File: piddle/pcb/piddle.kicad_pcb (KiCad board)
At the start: 2 copper layers, 139.2 x 138.5 mm, 87 parts, among them J1 Conn_01x03_Socket, J10 Conn_01x03_Socket, J11 Conn_01x03_Socket, J12 Conn_01x03_Socket, J13 Conn_01x03_Socket, J14 Conn_01x03_Socket, J15 Conn_01x03_Socket, J16 infrared receiver, J17 5v power, J18 3v3 power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

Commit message: Connect all components
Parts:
- added J25: JST power 3, Connector_JST:JST_PH_S2B-PH-K_1x02_P2.00mm_Horizontal, F.Cu at (41.7, 80.7)
- J17, J19: value 5v power -> 5v
- J18: value 3v3 power -> 3v3
- J22: renamed from LED v jumper
- moved J22 80.3 mm to (98.6, 136.6), turned to 90 degrees
- moved J21 50.8 mm to (146.6, 60.6), turned to 132 degrees
- moved R13 5.00 mm to (70.3, 126.8)
- moved R2 5.00 mm to (129.7, 126.8)
- moved R15 5.00 mm to (100.0, 140.0)
- moved R6 5.00 mm to (123.5, 67.6)
- moved R9 5.00 mm to (76.5, 67.6)
- moved R11 5.00 mm to (60.2, 95.8)
- moved R4 5.00 mm to (139.8, 95.8)
- moved R5 5.00 mm to (134.6, 80.0)
- moved R10 5.00 mm to (65.4, 80.0)
- moved R7 5.00 mm to (108.3, 60.9)
- moved R8 5.00 mm to (91.7, 60.9)
- moved R1 5.00 mm to (116.3, 136.5)
- moved R14 5.00 mm to (83.7, 136.5)
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- renumbered 34 to J23
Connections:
- J23 pad 1: /GPIO34 -> /GPIO35
- J23 pad 2: /GPIO39 -> /GPIO34
- J4 pad 2: Net-(D4-DIN) -> Net-(D4-DOUT)
- J6 pad 2: Net-(D6-DIN) -> Net-(D6-DOUT)
- R4 pad 2: Net-(D4-DOUT) -> Net-(D4-DIN)
- R6 pad 2: Net-(D6-DOUT) -> Net-(D6-DIN)
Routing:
- net /4.3V: track 0.00 -> 451.9 mm
- net +5V: track 0.00 -> 280.0 mm
- net +3.3V: track 0.00 -> 74.9 mm
- net /GPIO19: track 0.00 -> 49.5 mm
- net /GPIO21: track 0.00 -> 47.5 mm
- net /GPIO18: track 0.00 -> 46.3 mm
- net /GPIO35: track 0.00 -> 44.4 mm
- net /GPIO36: track 0.00 -> 42.0 mm
- net /GPIO5: track 0.00 -> 41.3 mm
- net /GPIO34: track 0.00 -> 40.8 mm
- net /GPIO33: track 0.00 -> 39.2 mm
- net /GPIO32: track 0.00 -> 39.0 mm
- net /GPIO25: track 0.00 -> 35.3 mm
- net /GPIO17: track 0.00 -> 34.1 mm
- net /GPIO39: track 0.00 -> 30.3 mm
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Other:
- board text added: "34"
- board text added: "35"
- board text added: "Brandon Skari"
- board text added: "LED v"
- board text added: "Phonic Bloom 2.0"
- board text added: "Phonic Bloom 2.0 Brandon Skari github.com/apogaea/piddle"
- board text added: "github.com/apogaea/piddle"

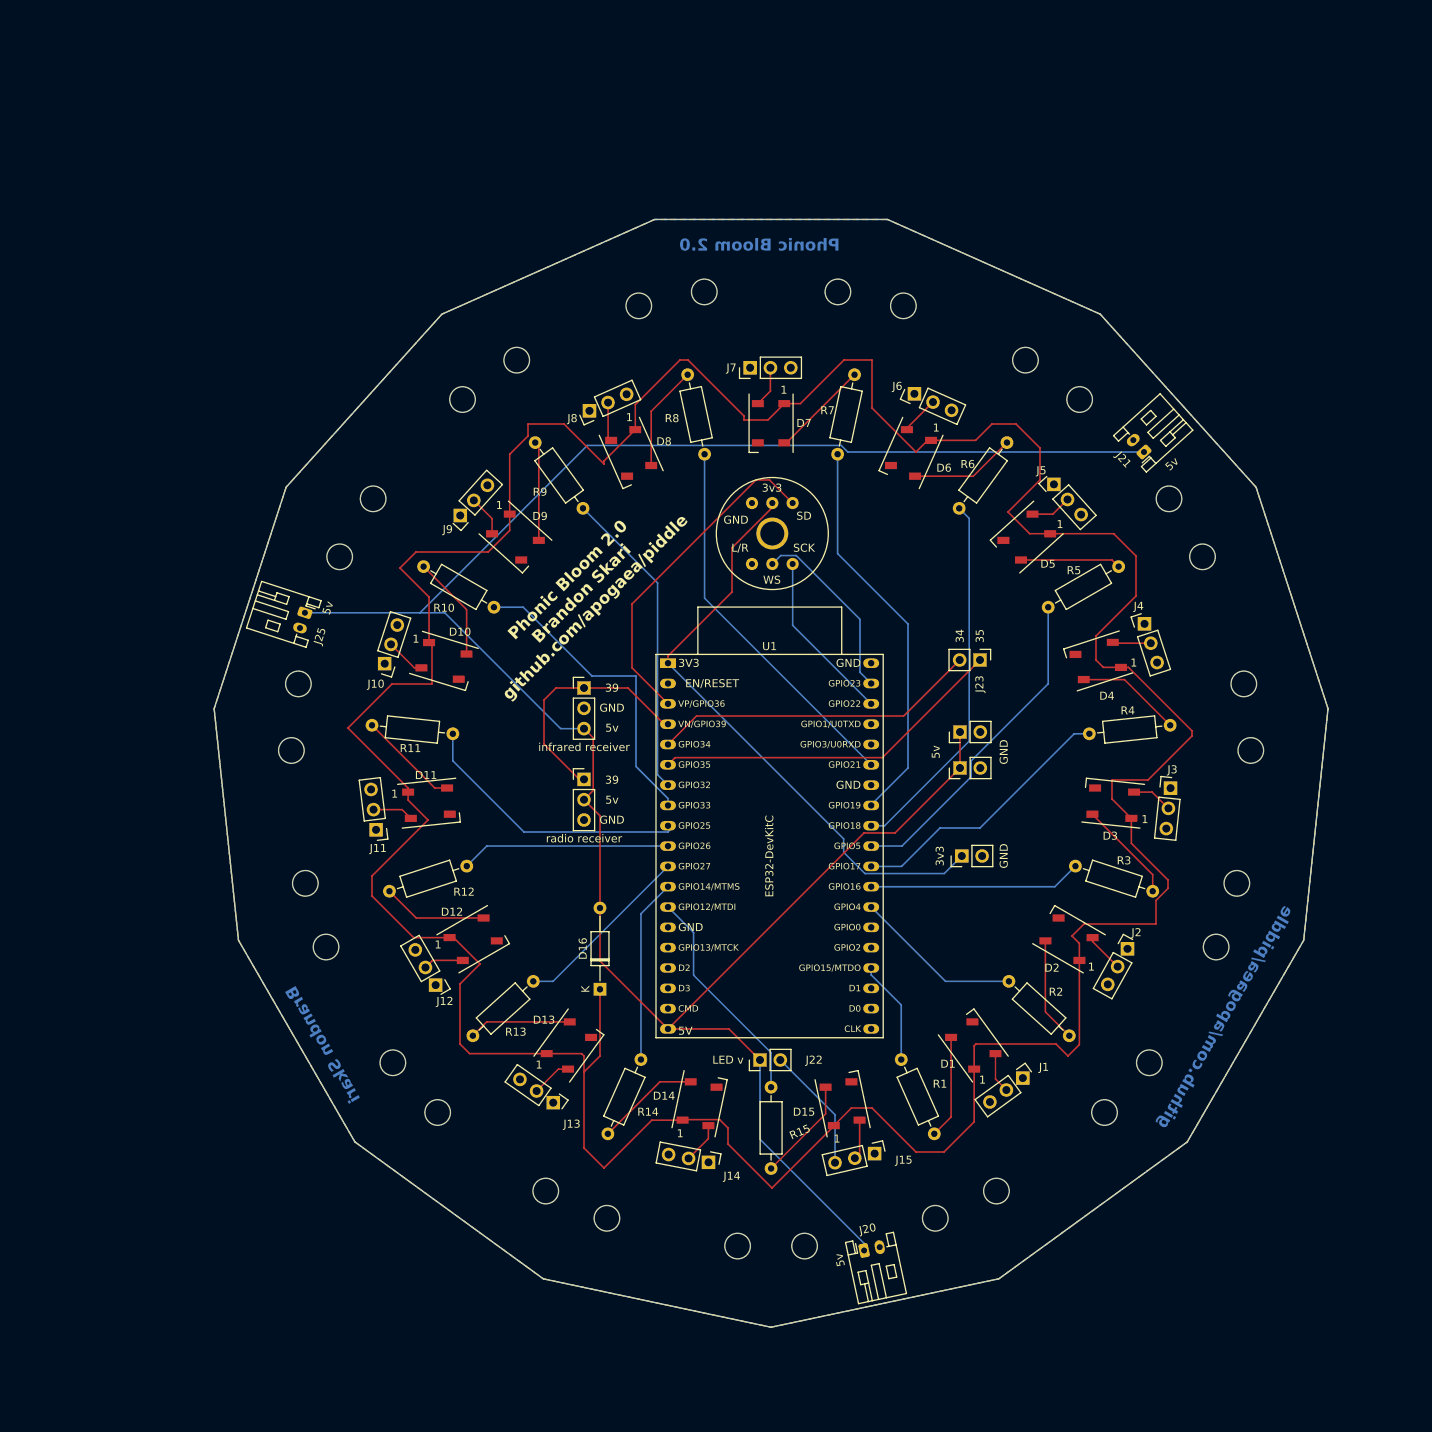
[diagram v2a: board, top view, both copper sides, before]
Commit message: Rotate LED solder pads and update to workwith KiCad 9
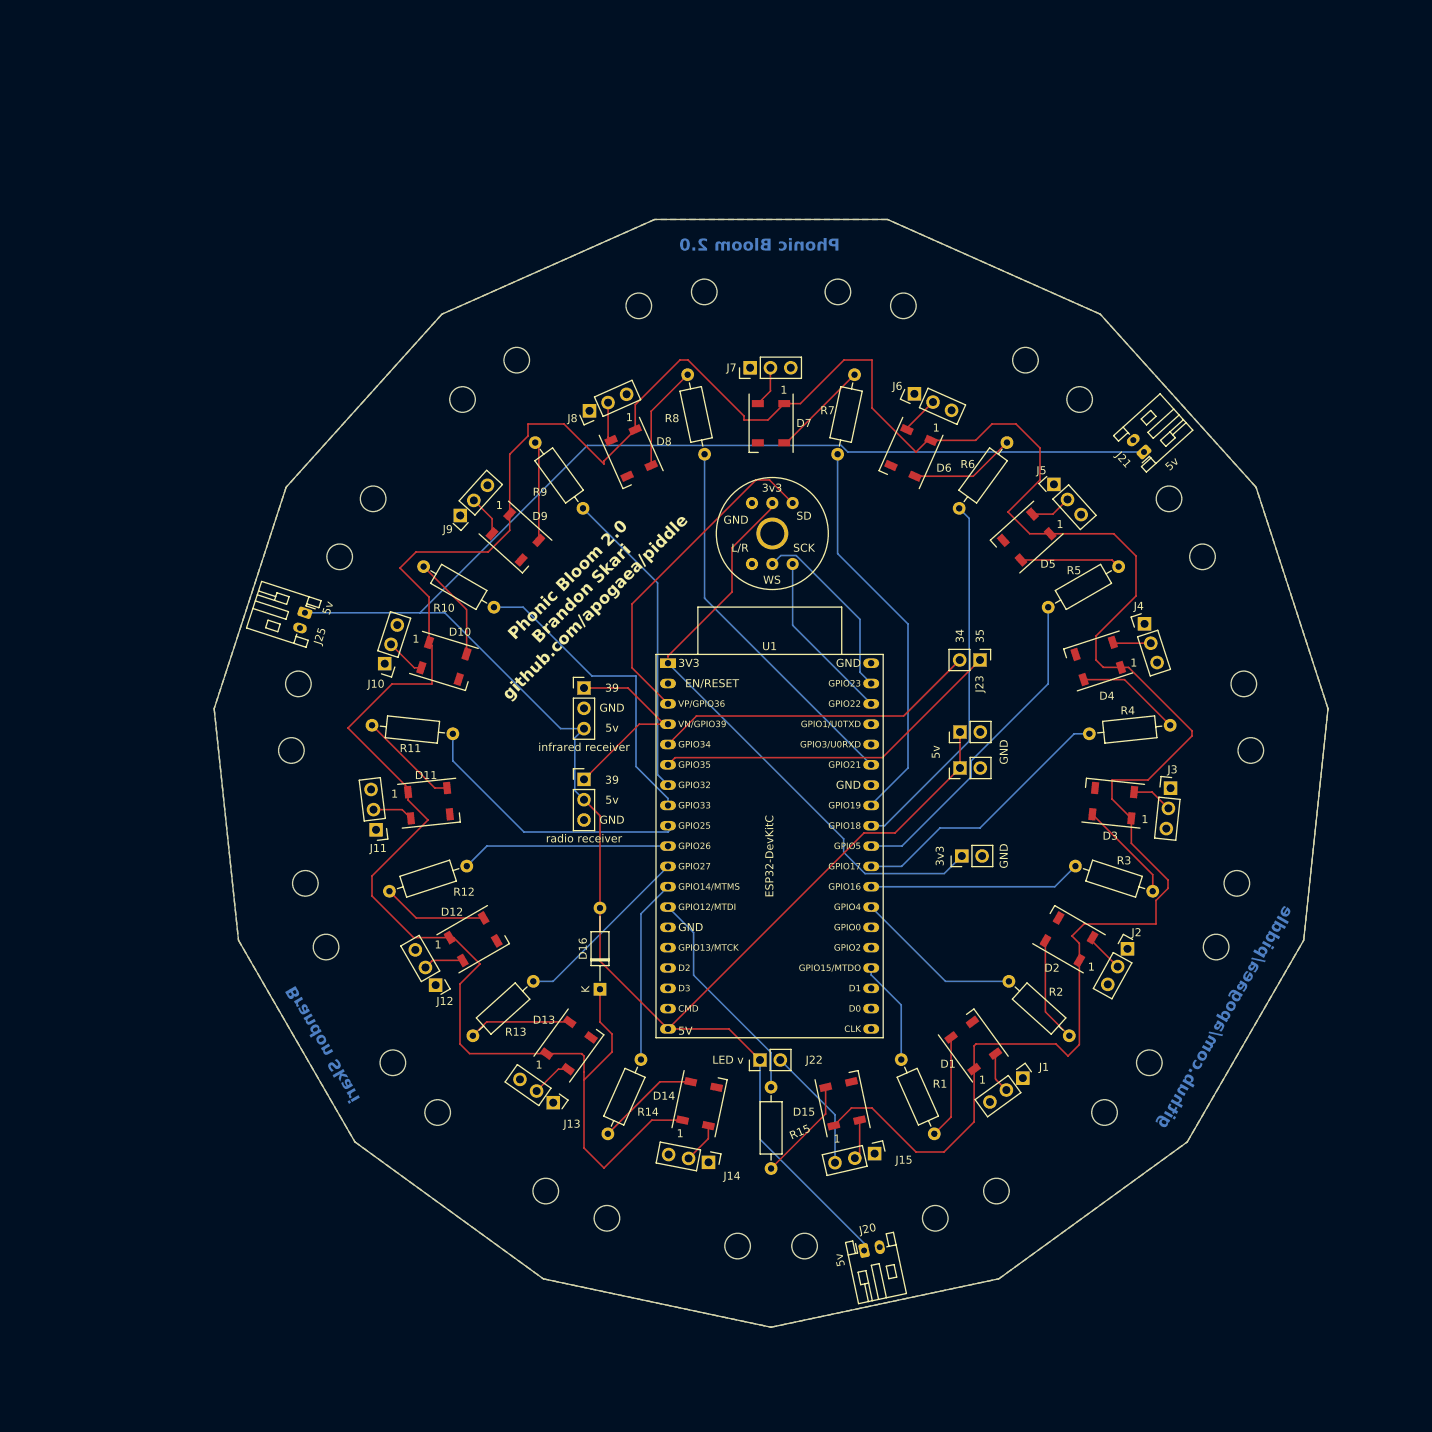
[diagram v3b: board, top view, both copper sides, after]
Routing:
- net /4.3V: track 451.9 -> 427.3 mm
- net /GPIO39: track 30.3 -> 25.7 mm

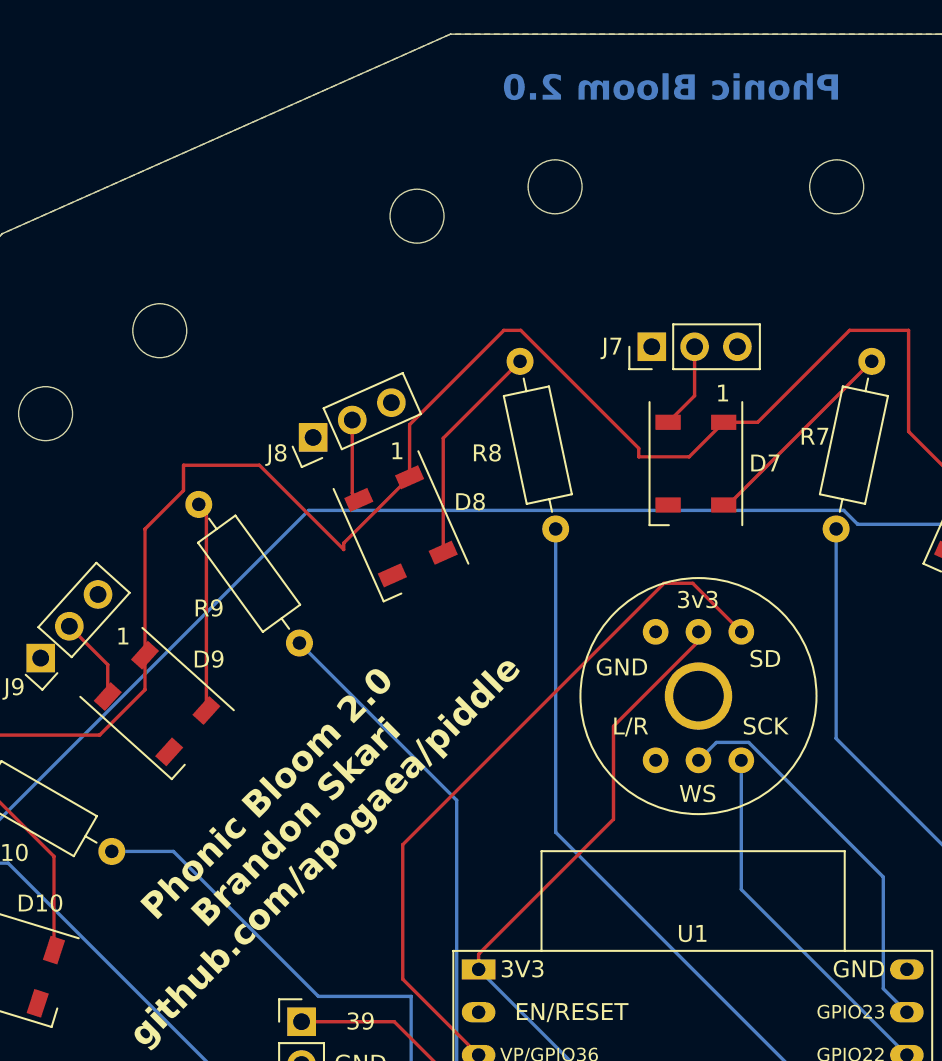
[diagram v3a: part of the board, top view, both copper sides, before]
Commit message: Update version on silkscreen
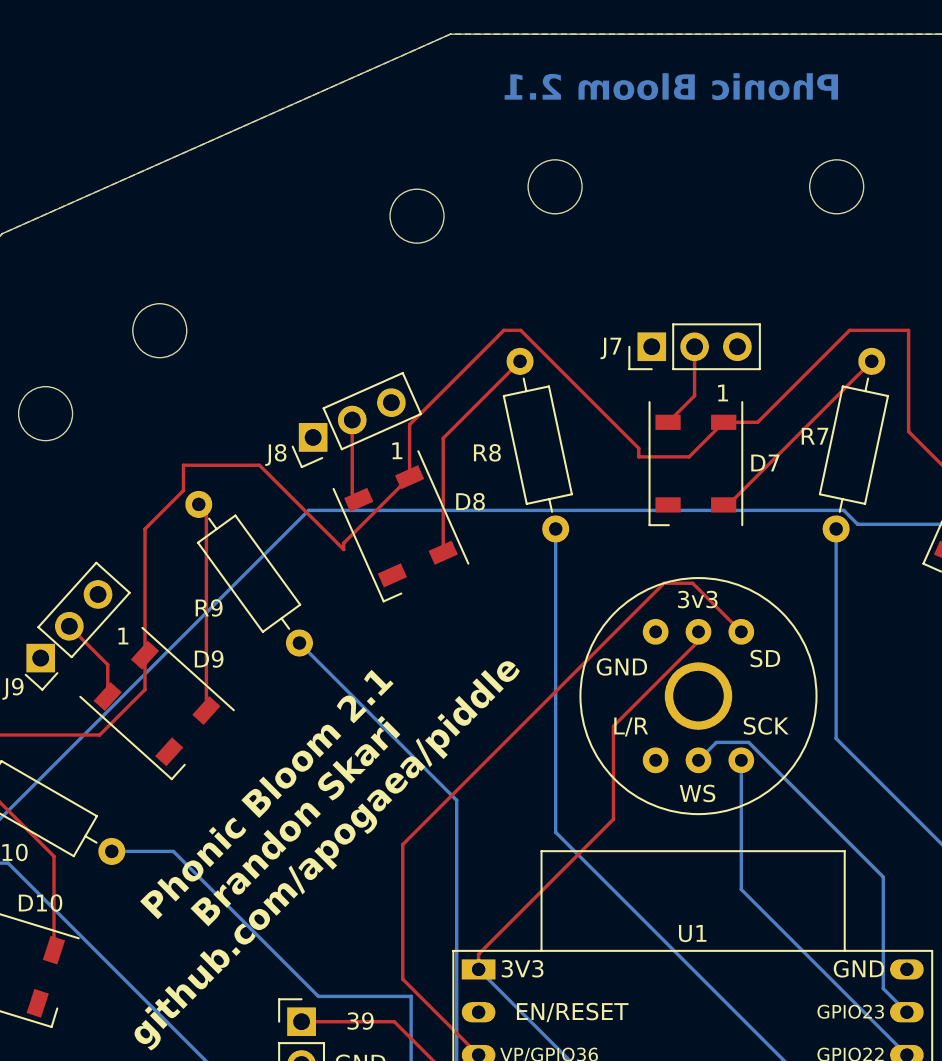
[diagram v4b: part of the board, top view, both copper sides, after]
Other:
- board text added: "Phonic Bloom 2.1"
- board text added: "Phonic Bloom 2.1 Brandon Skari github.com/apogaea/piddle"
- board text removed: "Phonic Bloom 2.0"
- board text removed: "Phonic Bloom 2.0 Brandon Skari github.com/apogaea/piddle"
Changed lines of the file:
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@@
 		)
 	)
-	(gr_text "Phonic Bloom 2.0"
+	(gr_text "Phonic Bloom 2.1"
 		(at 108.61328 35.596343 0)
 		(layer "B.Cu")
@@
 		)
 	)
-	(gr_text "Phonic Bloom 2.0\nBrandon Skari\ngithub.com/apogaea/piddle"
+	(gr_text "Phonic Bloom 2.1\nBrandon Skari\ngithub.com/apogaea/piddle"
 		(at 78.61328 80.596343 45)
 		(layer "F.SilkS")
